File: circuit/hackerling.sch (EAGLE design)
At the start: 38 parts, among them IC1 MCP23017SP, IC2 MCP2300X/P, IC3 MIC5219BM5, SW2 SWITCH_B13EH, U1 MMA8452Q, U2 LCD-16X2NOSILK, U3 ARDUINOR3-BPLACE, U5 PCA9306, U7 POT

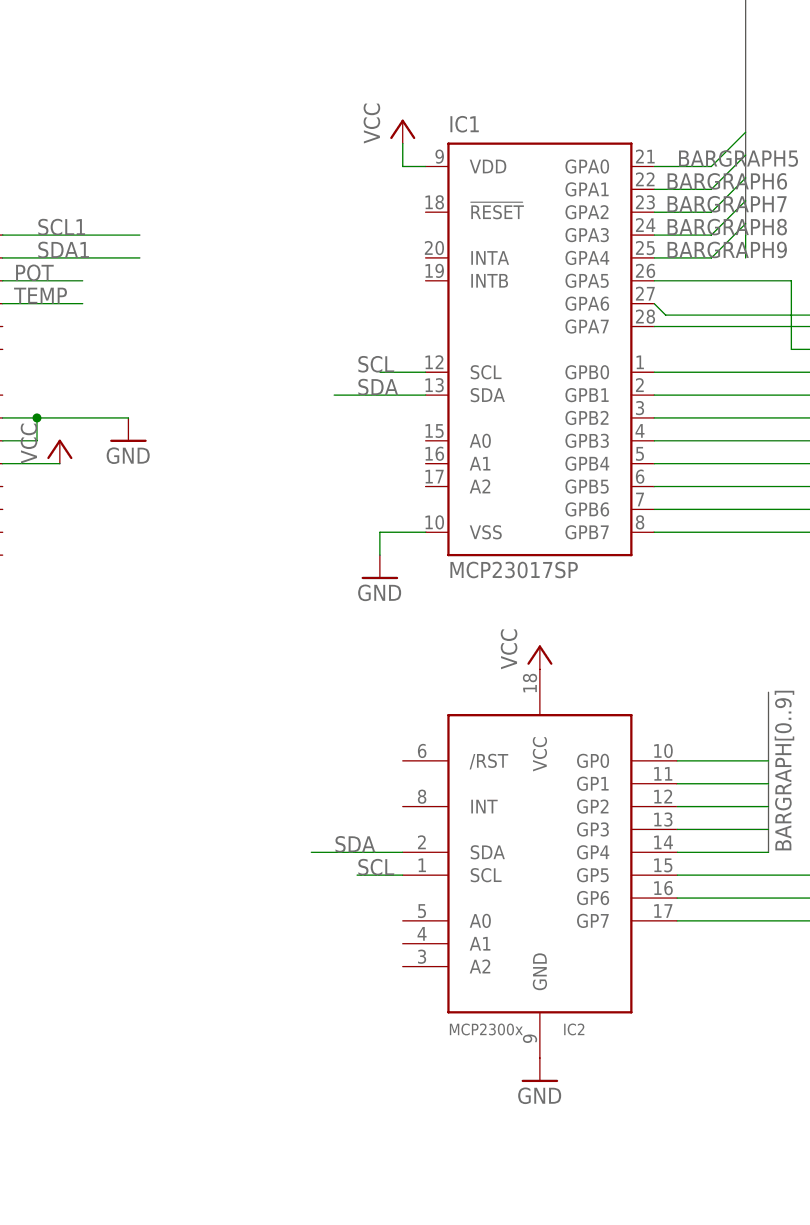
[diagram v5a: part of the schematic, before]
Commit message: changing accelerometer, adding hooked up address pins
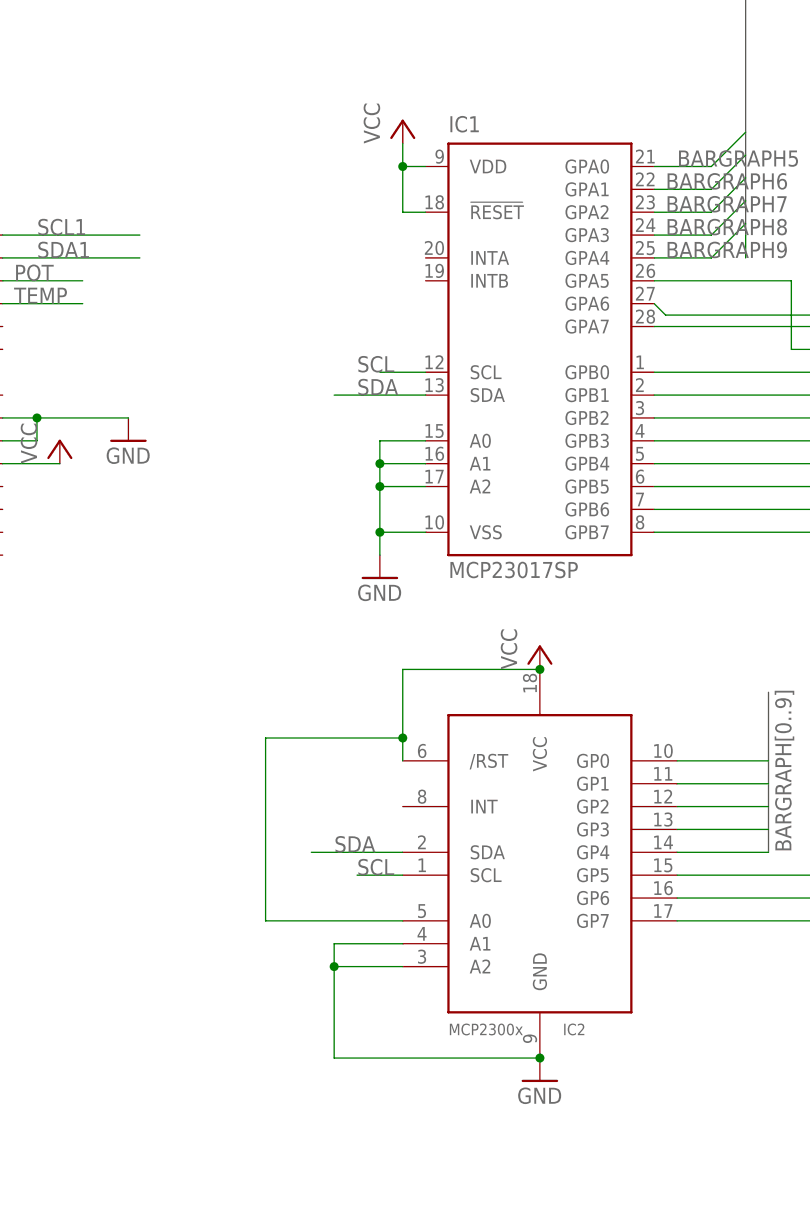
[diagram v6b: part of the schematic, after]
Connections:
- net GND: now also IC1.A0, IC1.A1, IC1.A2, IC2.A1, IC2.A2
- net VCC: now also IC1.!RESET, IC2./RST, IC2.A0
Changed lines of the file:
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@@
 <pinref part="IC2" gate="G$1" pin="GND"/>
 <pinref part="GND2" gate="1" pin="GND"/>
+<pinref part="IC2" gate="G$1" pin="A1"/>
+<wire x1="129.54" y1="-20.32" x2="121.92" y2="-20.32" width="0.1524" layer="91"/>
+<wire x1="121.92" y1="-20.32" x2="121.92" y2="-22.86" width="0.1524" layer="91"/>
+<pinref part="IC2" gate="G$1" pin="A2"/>
+<wire x1="129.54" y1="-22.86" x2="121.92" y2="-22.86" width="0.1524" layer="91"/>
+<junction x="121.92" y="-22.86"/>
+<wire x1="121.92" y1="-22.86" x2="121.92" y2="-33.02" width="0.1524" layer="91"/>
+<wire x1="121.92" y1="-33.02" x2="144.78" y2="-33.02" width="0.1524" layer="91"/>
+<junction x="144.78" y="-33.02"/>
 </segment>
 <segment>
@@
 <wire x1="132.08" y1="25.4" x2="127" y2="25.4" width="0.1524" layer="91"/>
 <wire x1="127" y1="25.4" x2="127" y2="22.86" width="0.1524" layer="91"/>
+<pinref part="IC1" gate="G$1" pin="A0"/>
+<wire x1="132.08" y1="35.56" x2="127" y2="35.56" width="0.1524" layer="91"/>
+<wire x1="127" y1="35.56" x2="127" y2="33.02" width="0.1524" layer="91"/>
+<junction x="127" y="25.4"/>
+<pinref part="IC1" gate="G$1" pin="A1"/>
+<wire x1="127" y1="33.02" x2="127" y2="30.48" width="0.1524" layer="91"/>
+<wire x1="127" y1="30.48" x2="127" y2="25.4" width="0.1524" layer="91"/>
+<wire x1="132.08" y1="33.02" x2="127" y2="33.02" width="0.1524" layer="91"/>
+<junction x="127" y="33.02"/>
+<pinref part="IC1" gate="G$1" pin="A2"/>
+<wire x1="132.08" y1="30.48" x2="127" y2="30.48" width="0.1524" layer="91"/>
+<junction x="127" y="30.48"/>
 </segment>
 <segment>
@@
 <pinref part="IC2" gate="G$1" pin="VCC"/>
 <pinref part="P+5" gate="VCC" pin="VCC"/>
+<pinref part="IC2" gate="G$1" pin="/RST"/>
+<wire x1="144.78" y1="10.16" x2="129.54" y2="10.16" width="0.1524" layer="91"/>
+<wire x1="129.54" y1="10.16" x2="129.54" y2="2.54" width="0.1524" layer="91"/>
+<junction x="144.78" y="10.16"/>
+<pinref part="IC2" gate="G$1" pin="A0"/>
+<wire x1="129.54" y1="2.54" x2="129.54" y2="0" width="0.1524" layer="91"/>
+<wire x1="129.54" y1="-17.78" x2="114.3" y2="-17.78" width="0.1524" layer="91"/>
+<wire x1="114.3" y1="-17.78" x2="114.3" y2="2.54" width="0.1524" layer="91"/>
+<wire x1="114.3" y1="2.54" x2="129.54" y2="2.54" width="0.1524" layer="91"/>
+<junction x="129.54" y="2.54"/>
 </segment>
 <segment>
@@
 <wire x1="132.08" y1="66.04" x2="129.54" y2="66.04" width="0.1524" layer="91"/>
 <wire x1="129.54" y1="66.04" x2="129.54" y2="68.58" width="0.1524" layer="91"/>
+<pinref part="IC1" gate="G$1" pin="!RESET"/>
+<wire x1="132.08" y1="60.96" x2="129.54" y2="60.96" width="0.1524" layer="91"/>
+<wire x1="129.54" y1="60.96" x2="129.54" y2="66.04" width="0.1524" layer="91"/>
+<junction x="129.54" y="66.04"/>
 </segment>
 <segment>
